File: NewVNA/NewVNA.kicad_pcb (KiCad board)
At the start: 2 copper layers, 48.9 x 39.1 mm, 14 parts, among them J4 Conn_01x03

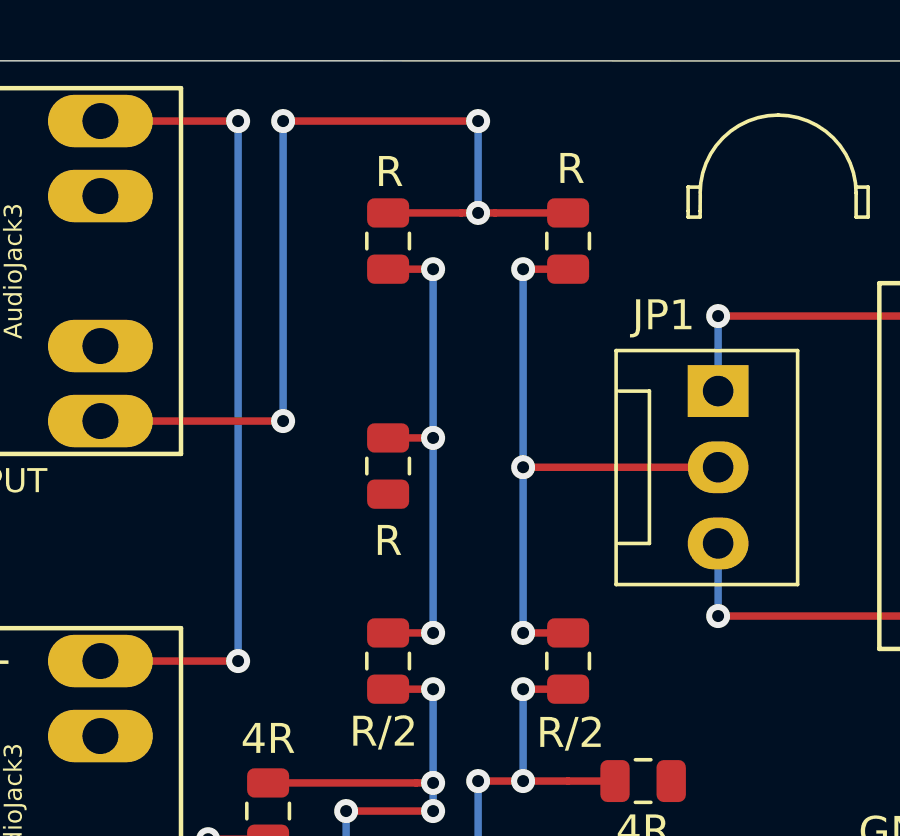
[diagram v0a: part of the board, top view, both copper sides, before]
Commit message: cleaning up the pcb schematic and some comments on the code
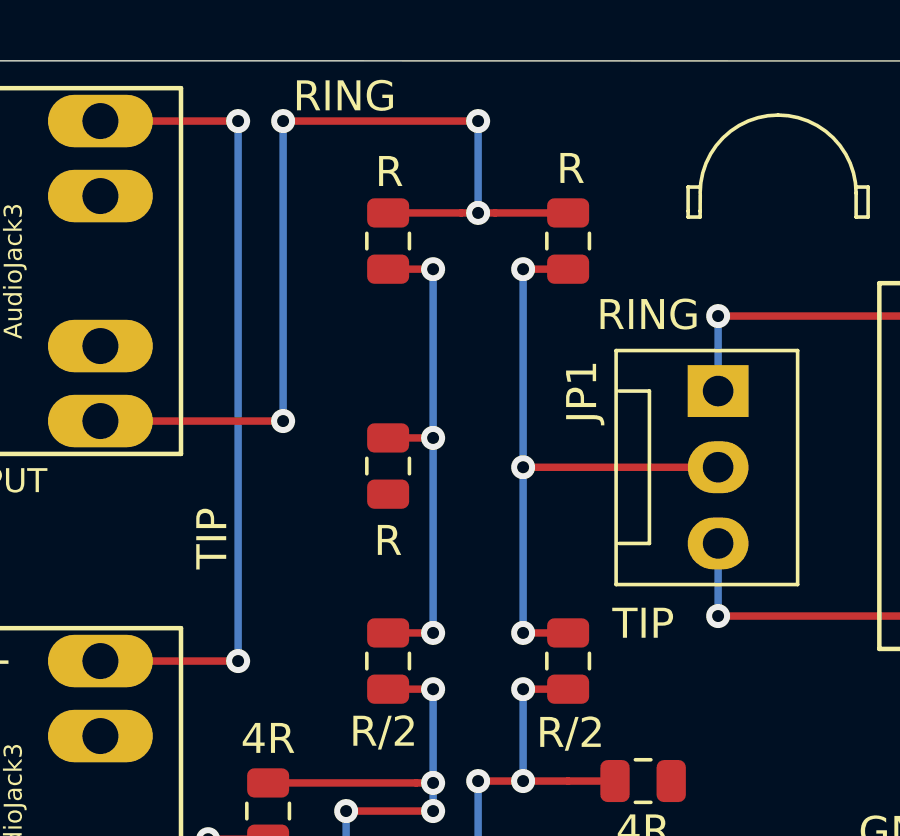
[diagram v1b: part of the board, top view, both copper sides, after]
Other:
- board text added: "RING"
- board text added: "TIP"
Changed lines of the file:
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@@
   (general
     (thickness 1.6)
-    (drawings 24)
+    (drawings 28)
     (tracks 102)
     (zones 0)
@@
     (descr "3-pin CPU fan Through hole pin header, see http://www.formfactors.org/developer%5Cspecs%5Crev1_2_public.pdf")
     (tags "pin header 3-pin CPU fan")
-    (fp_text reference JP1 (at -2.5228 1.8152 180) (layer F.SilkS)
+    (fp_text reference JP1 (at 0.02 4.53 90) (layer F.SilkS)
       (effects (font (size 1 1) (thickness 0.15)))
     )
@@
     )
   )
+  (gr_text RING (at 45.55 26.18) (layer F.SilkS)
+    (effects (font (size 1 1) (thickness 0.15)))
+  )
+  (gr_text TIP (at 41.14 40.91 90) (layer F.SilkS)
+    (effects (font (size 1 1) (thickness 0.15)))
+  )
+  (gr_text TIP (at 55.51 43.76) (layer F.SilkS)
+    (effects (font (size 1 1) (thickness 0.15)))
+  )
+  (gr_text RING (at 55.67 33.47) (layer F.SilkS)
+    (effects (font (size 1 1) (thickness 0.15)))
+  )
   (gr_line (start 76.1492 25) (end 27.3 24.99) (layer Edge.Cuts) (width 0.05))
